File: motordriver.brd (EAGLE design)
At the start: 101.6 x 83.8 mm, 100 parts, among them J1 CONNECTOR_MOTORS, J10 HEADER_1X3, J11 HEADER_1X3, J2 CONNECTOR_MOTORS, J3 CONNECTOR_MOTORS, J4 CONNECTOR_MOTORS, J5 HEADER_1X3, J6 HEADER_1X3, J7 HEADER_1X3, J8 HEADER_1X3, J9 CONNECTOR_MOTORS, Q1 MOSFET, Q10 MOSFET, Q11 MOSFET, Q12 MOSFET, Q13 MOSFET, Q14 MOSFET, Q15 MOSFET, Q16 MOSFET, Q2 MOSFET, Q3 MOSFET, Q4 MOSFET, Q5 MOSFET, Q6 MOSFET, Q7 MOSFET, Q8 MOSFET, Q9 MOSFET, U1 74XX139_PDIP, U10 IR2111_PDIP, U11 IR2111_PDIP, U12 7812_TO220, U2 TL084_PDIP, U3 7812_TO220, U4 IR2111_PDIP, U5 IR2111_PDIP, U6 IR2111_PDIP, U7 IR2111_PDIP, U8 IR2111_PDIP, U9 IR2111_PDIP

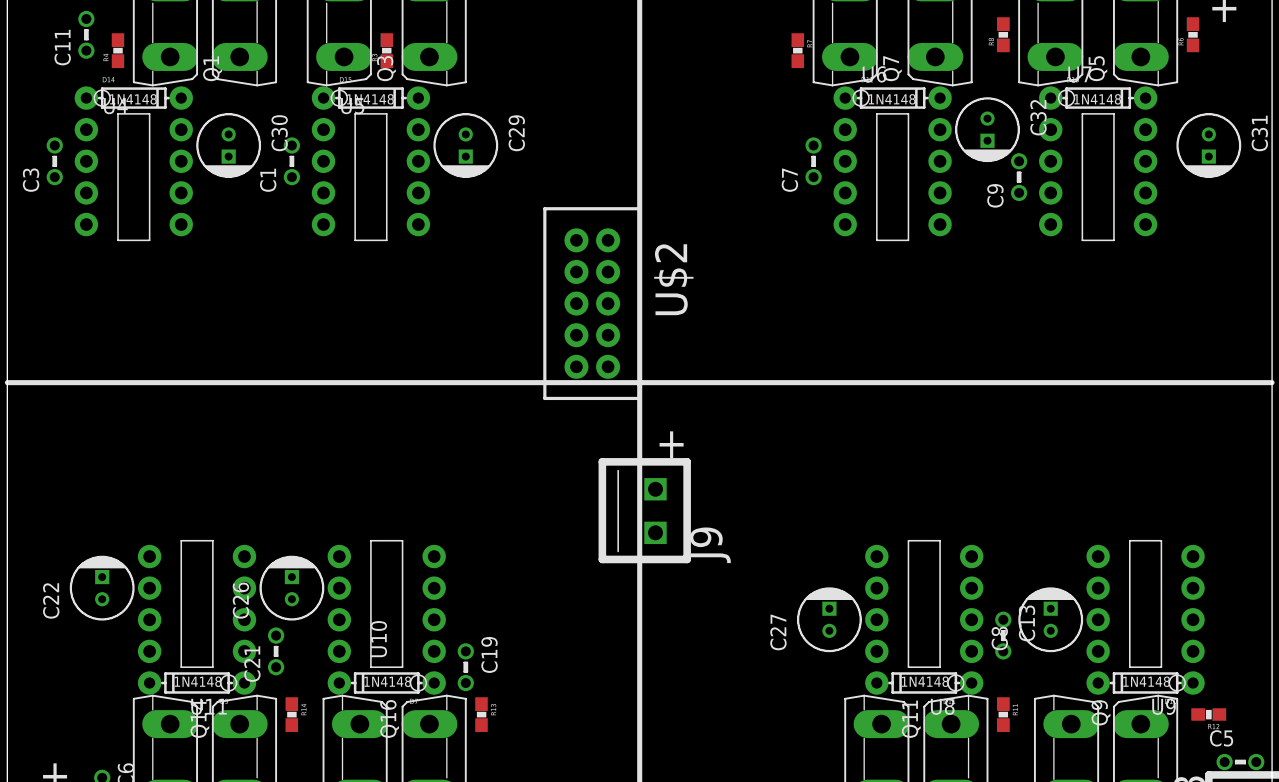
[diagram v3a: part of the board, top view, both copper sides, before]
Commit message: double fixed dodes
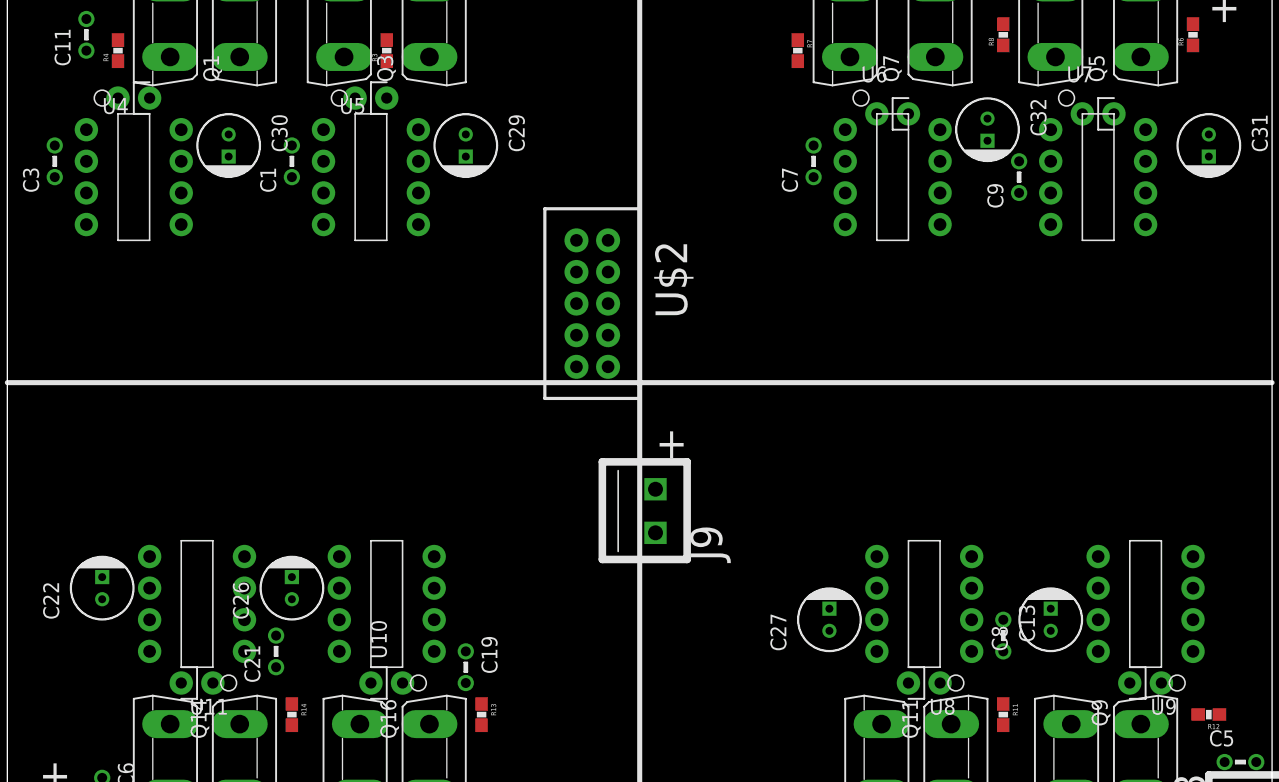
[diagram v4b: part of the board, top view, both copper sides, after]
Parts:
- moved D12 1.80 mm to (69.8, 63.5), turned to 90 degrees
- moved D13 1.80 mm to (86.4, 63.5), turned to 90 degrees
- moved D11 1.27 mm to (74.9, 17.8), turned to 270 degrees
- moved D9 1.27 mm to (16.5, 17.8), turned to 270 degrees
- moved D14 1.27 mm to (8.89, 64.8), turned to 90 degrees
- moved D15 1.27 mm to (27.9, 64.8), turned to 90 degrees
- moved D7 1.27 mm to (31.8, 17.8), turned to 270 degrees
- moved D10 1.27 mm to (92.7, 17.8), turned to 270 degrees
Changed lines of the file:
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@@
 <?xml version="1.0" encoding="utf-8"?>
 <!DOCTYPE eagle SYSTEM "eagle.dtd">
-<eagle version="7.2.0">
+<eagle version="7.1.0">
 <drawing>
 <settings>
@@
 <element name="C9" library="motordriverslib" package="2DIP" value="CAP_1U" x="81.28" y="57.15"/>
 <element name="D1" library="motordriverslib" package="LED_0603" value="LED_SMT" x="-82.55" y="115.57"/>
-<element name="D10" library="motordriverslib" package="1N4148" value="1N4148" x="91.44" y="17.78" rot="R180"/>
-<element name="D11" library="motordriverslib" package="1N4148" value="1N4148" x="73.66" y="17.78" rot="R180"/>
-<element name="D12" library="motordriverslib" package="1N4148" value="1N4148" x="71.12" y="64.77"/>
-<element name="D13" library="motordriverslib" package="1N4148" value="1N4148" x="87.63" y="64.77"/>
-<element name="D14" library="motordriverslib" package="1N4148" value="1N4148" x="10.16" y="64.77"/>
-<element name="D15" library="motordriverslib" package="1N4148" value="1N4148" x="29.21" y="64.77"/>
-<element name="D7" library="motordriverslib" package="1N4148" value="1N4148" x="30.48" y="17.78" rot="R180"/>
-<element name="D9" library="motordriverslib" package="1N4148" value="1N4148" x="15.24" y="17.78" rot="R180"/>
+<element name="D10" library="motordriverslib" package="1N4148" value="1N4148" x="92.71" y="17.78" rot="R270"/>
+<element name="D11" library="motordriverslib" package="1N4148" value="1N4148" x="74.93" y="17.78" rot="R270"/>
+<element name="D12" library="motordriverslib" package="1N4148" value="1N4148" x="69.85" y="63.5" rot="R90"/>
+<element name="D13" library="motordriverslib" package="1N4148" value="1N4148" x="86.36" y="63.5" rot="R90"/>
+<element name="D14" library="motordriverslib" package="1N4148" value="1N4148" x="8.89" y="64.77" rot="R90"/>
+<element name="D15" library="motordriverslib" package="1N4148" value="1N4148" x="27.94" y="64.77" rot="R90"/>
+<element name="D7" library="motordriverslib" package="1N4148" value="1N4148" x="31.75" y="17.78" rot="R270"/>
+<element name="D9" library="motordriverslib" package="1N4148" value="1N4148" x="16.51" y="17.78" rot="R270"/>
 <element name="J1" library="motordriverslib" package="CONN_MOTOR" value="CONNECTOR_MOTORS" x="2.54" y="77.47"/>
 <element name="J10" library="motordriverslib" package="HEADER_1X3" value="HEADER_1X3" x="-63.5" y="110.49"/>
@@
 <contactref element="U2" pad="VCC"/>
 <contactref element="D1" pad="A"/>
-<wire x1="83.82" y1="62.23" x2="83.82" y2="64.77" width="0" layer="19" extent="1-1"/>
+<wire x1="83.82" y1="62.23" x2="86.36" y2="63.5" width="0" layer="19" extent="1-1"/>
 <wire x1="81.28" y1="59.69" x2="83.82" y2="62.23" width="0" layer="19" extent="1-1"/>
 <wire x1="67.31" y1="62.23" x2="81.28" y2="59.69" width="0" layer="19" extent="1-1"/>
-<wire x1="67.31" y1="64.77" x2="67.31" y2="62.23" width="0" layer="19" extent="1-1"/>
+<wire x1="69.85" y1="63.5" x2="67.31" y2="62.23" width="0" layer="19" extent="1-1"/>
 <wire x1="64.77" y1="60.96" x2="67.31" y2="62.23" width="0" layer="19" extent="1-1"/>
 <wire x1="80.01" y1="20.32" x2="81.28" y2="59.69" width="0" layer="19" extent="1-1"/>
 <wire x1="77.47" y1="20.32" x2="80.01" y2="20.32" width="0" layer="19" extent="1-1"/>
-<wire x1="77.47" y1="17.78" x2="77.47" y2="20.32" width="0" layer="19" extent="1-1"/>
+<wire x1="74.93" y1="17.78" x2="77.47" y2="20.32" width="0" layer="19" extent="1-1"/>
 <wire x1="95.25" y1="20.32" x2="80.01" y2="20.32" width="0" layer="19" extent="1-1"/>
-<wire x1="95.25" y1="17.78" x2="95.25" y2="20.32" width="0" layer="19" extent="1-1"/>
+<wire x1="92.71" y1="17.78" x2="95.25" y2="20.32" width="0" layer="19" extent="1-1"/>
 <wire x1="25.4" y1="62.23" x2="64.77" y2="60.96" width="0" layer="19" extent="1-1"/>
-<wire x1="25.4" y1="64.77" x2="25.4" y2="62.23" width="0" layer="19" extent="1-1"/>
+<wire x1="27.94" y1="64.77" x2="25.4" y2="62.23" width="0" layer="19" extent="1-1"/>
 <wire x1="22.86" y1="60.96" x2="25.4" y2="62.23" width="0" layer="19" extent="1-1"/>
 <wire x1="6.35" y1="62.23" x2="22.86" y2="60.96" width="0" layer="19" extent="1-1"/>
-<wire x1="6.35" y1="64.77" x2="6.35" y2="62.23" width="0" layer="19" extent="1-1"/>
+<wire x1="8.89" y1="64.77" x2="6.35" y2="62.23" width="0" layer="19" extent="1-1"/>
 <wire x1="3.81" y1="60.96" x2="6.35" y2="62.23" width="0" layer="19" extent="1-1"/>
 <wire x1="21.59" y1="21.59" x2="22.86" y2="60.96" width="0" layer="19" extent="1-1"/>
 <wire x1="19.05" y1="20.32" x2="21.59" y2="21.59" width="0" layer="19" extent="1-1"/>
-<wire x1="19.05" y1="17.78" x2="19.05" y2="20.32" width="0" layer="19" extent="1-1"/>
+<wire x1="16.51" y1="17.78" x2="19.05" y2="20.32" width="0" layer="19" extent="1-1"/>
 <wire x1="34.29" y1="20.32" x2="21.59" y2="21.59" width="0" layer="19" extent="1-1"/>
-<wire x1="34.29" y1="17.78" x2="34.29" y2="20.32" width="0" layer="19" extent="1-1"/>
-<wire x1="36.83" y1="17.78" x2="34.29" y2="17.78" width="0" layer="19" extent="1-1"/>
-<wire x1="-43.18" y1="12.7" x2="19.05" y2="17.78" width="0" layer="19" extent="1-1"/>
+<wire x1="31.75" y1="17.78" x2="34.29" y2="20.32" width="0" layer="19" extent="1-1"/>
+<wire x1="36.83" y1="17.78" x2="31.75" y2="17.78" width="0" layer="19" extent="1-1"/>
+<wire x1="-43.18" y1="12.7" x2="16.51" y2="17.78" width="0" layer="19" extent="1-1"/>
 <wire x1="-69.85" y1="52.07" x2="-43.18" y2="12.7" width="0" layer="19" extent="1-1"/>
 <wire x1="-92.71" y1="10.16" x2="-69.85" y2="52.07" width="0" layer="19" extent="1-1"/>
@@
 <contactref element="D15" pad="C"/>
 <wire x1="33.02" y1="62.23" x2="36.83" y2="61.849" width="0" layer="19" extent="1-1"/>
-<wire x1="33.02" y1="64.77" x2="33.02" y2="62.23" width="0" layer="19" extent="1-1"/>
+<wire x1="30.48" y1="64.77" x2="33.02" y2="62.23" width="0" layer="19" extent="1-1"/>
 </signal>
 <signal name="N$15">
@@
 <contactref element="D14" pad="C"/>
 <wire x1="13.97" y1="62.23" x2="17.78" y2="61.849" width="0" layer="19" extent="1-1"/>
-<wire x1="13.97" y1="64.77" x2="13.97" y2="62.23" width="0" layer="19" extent="1-1"/>
+<wire x1="11.43" y1="64.77" x2="13.97" y2="62.23" width="0" layer="19" extent="1-1"/>
 </signal>
 <signal name="N$26">
@@
 <contactref element="D12" pad="C"/>
 <wire x1="74.93" y1="62.23" x2="78.74" y2="63.119" width="0" layer="19" extent="1-1"/>
-<wire x1="74.93" y1="64.77" x2="74.93" y2="62.23" width="0" layer="19" extent="1-1"/>
+<wire x1="72.39" y1="63.5" x2="74.93" y2="62.23" width="0" layer="19" extent="1-1"/>
 </signal>
 <signal name="N$31">
@@
 <contactref element="D13" pad="C"/>
 <wire x1="91.44" y1="62.23" x2="96.52" y2="61.849" width="0" layer="19" extent="1-1"/>
-<wire x1="91.44" y1="64.77" x2="91.44" y2="62.23" width="0" layer="19" extent="1-1"/>
+<wire x1="88.9" y1="63.5" x2="91.44" y2="62.23" width="0" layer="19" extent="1-1"/>
 </signal>
 <signal name="N$39">
@@
 <contactref element="C27" pad="+"/>
 <contactref element="D11" pad="C"/>
-<wire x1="69.85" y1="17.78" x2="69.85" y2="20.32" width="0" layer="19" extent="1-1"/>
+<wire x1="72.39" y1="17.78" x2="69.85" y2="20.32" width="0" layer="19" extent="1-1"/>
 <wire x1="66.04" y1="21.971" x2="69.85" y2="20.32" width="0" layer="19" extent="1-1"/>
 </signal>
@@
 <contactref element="D10" pad="C"/>
 <contactref element="C8" pad="+"/>
-<wire x1="87.63" y1="17.78" x2="87.63" y2="20.32" width="0" layer="19" extent="1-1"/>
+<wire x1="90.17" y1="17.78" x2="87.63" y2="20.32" width="0" layer="19" extent="1-1"/>
 <wire x1="83.82" y1="21.971" x2="87.63" y2="20.32" width="0" layer="19" extent="1-1"/>
 </signal>
@@
 <contactref element="C26" pad="+"/>
 <contactref element="D7" pad="C"/>
-<wire x1="26.67" y1="17.78" x2="26.67" y2="20.32" width="0" layer="19" extent="1-1"/>
+<wire x1="29.21" y1="17.78" x2="26.67" y2="20.32" width="0" layer="19" extent="1-1"/>
 <wire x1="22.86" y1="24.511" x2="26.67" y2="20.32" width="0" layer="19" extent="1-1"/>
 </signal>
@@
 <contactref element="C22" pad="+"/>
 <contactref element="D9" pad="C"/>
-<wire x1="11.43" y1="17.78" x2="11.43" y2="20.32" width="0" layer="19" extent="1-1"/>
+<wire x1="13.97" y1="17.78" x2="11.43" y2="20.32" width="0" layer="19" extent="1-1"/>
 <wire x1="7.62" y1="24.511" x2="11.43" y2="20.32" width="0" layer="19" extent="1-1"/>
 </signal>

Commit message: More PCB tinkering
Routing will commence soon
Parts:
- removed S1: ROCKER_THRU, motordriverslib:SW_THRU
- moved C2 170.8 mm to (58.4, 22.9), turned to 90 degrees
- moved C4 168.3 mm to (48.3, 27.9), turned to 90 degrees
- moved U3 145.9 mm to (47.0, 21.6), turned to 180 degrees
- moved C25 136.6 mm to (61.0, 12.7), turned to 90 degrees
- moved U2 135.0 mm to (88.9, 48.3), turned to 270 degrees
- moved U$1 128.9 mm to (47.0, 34.3), turned to 180 degrees
- moved U12 123.0 mm to (21.6, 40.6)
- moved C18 103.6 mm to (54.6, 31.8)
- moved U1 91.1 mm to (54.6, 58.4)
- moved C17 44.4 mm to (7.62, 41.9)
- moved J9 30.2 mm to (59.7, 2.54), turned to 90 degrees
- moved D14 2.54 mm to (6.35, 64.8)
- moved D15 2.54 mm to (30.5, 64.8)
- moved U$2 2.54 mm to (44.5, 48.3)
- moved D12 1.27 mm to (69.8, 64.8)
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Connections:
- net VIN_RAW: now also U3.IN; no longer S1.+
- net V_IN: no longer S1.-, U3.IN

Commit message: Dank
ass
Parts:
- moved J8 114.6 mm to (57.1, 68.6), turned to 90 degrees
- moved J7 86.9 mm to (41.9, 71.1), turned to 90 degrees
- moved J9 61.3 mm to (99.1, 49.5), turned to 180 degrees
- moved U3 52.3 mm to (92.7, 47.0), turned to 90 degrees
- moved C25 42.3 mm to (83.8, 48.3), turned to 270 degrees
- moved U2 38.7 mm to (53.3, 33.0), turned to 180 degrees
- moved R7 30.7 mm to (94.0, 64.8), turned to 90 degrees
- moved C2 30.3 mm to (74.9, 48.3), turned to 180 degrees
- moved Q7 28.1 mm to (96.5, 71.1), turned to 270 degrees
- moved U$1 28.1 mm to (44.5, 6.35)
- moved Q6 25.3 mm to (66.0, 81.3), turned to 180 degrees
- moved C18 20.5 mm to (52.1, 11.4)
- moved R8 20.3 mm to (59.7, 69.8)
- moved R6 20.3 mm to (74.9, 69.8)
- moved J2 19.4 mm to (80.0, 81.3), turned to 270 degrees
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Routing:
- net N$27: track 0.00 -> 22.6 mm
- net N$20: track 0.00 -> 21.4 mm
- net N$19: track 0.00 -> 19.8 mm
- net N$16: track 0.00 -> 18.2 mm
- net Y_PWM_B: track 0.00 -> 14.3 mm
- net Y_PWM_A: track 0.00 -> 13.3 mm
- net VCC_12V: track 0.00 -> 10.8 mm
- net N$25: track 0.00 -> 9.96 mm
- net N$13: track 0.00 -> 5.85 mm
- net GND: track 0.00 -> 5.68 mm
- net N$15: track 0.00 -> 4.80 mm
- net N$26: track 0.00 -> 4.80 mm
- net N$17: track 0.00 -> 4.73 mm
- net N$24: track 0.00 -> 4.20 mm
- net N$14: track 0.00 -> 4.19 mm
